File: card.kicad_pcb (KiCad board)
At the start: 2 copper layers, 38.6 x 52.3 mm, 92 parts, among them J1 Conn_01x20_Male, J2 HDMI_A, J3 Conn_01x20_Male, J4 USB_B_Micro, Q1 MMBT3906, Q3 MMBT3906, Q4 MMBT3904, SW1 SW_DPST_x2, U1 SPX3819-1.8, U2 IMP811REUS-T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

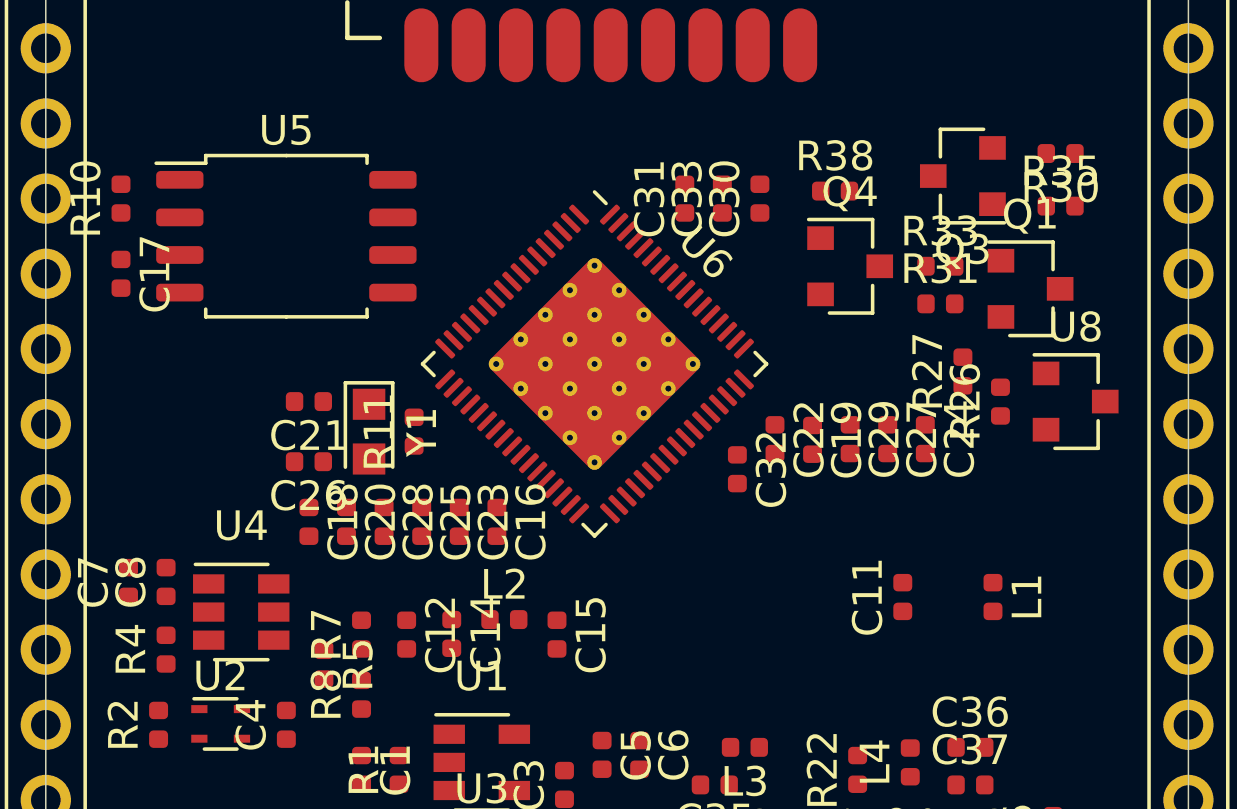
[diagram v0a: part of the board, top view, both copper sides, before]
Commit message: started routing the PCB
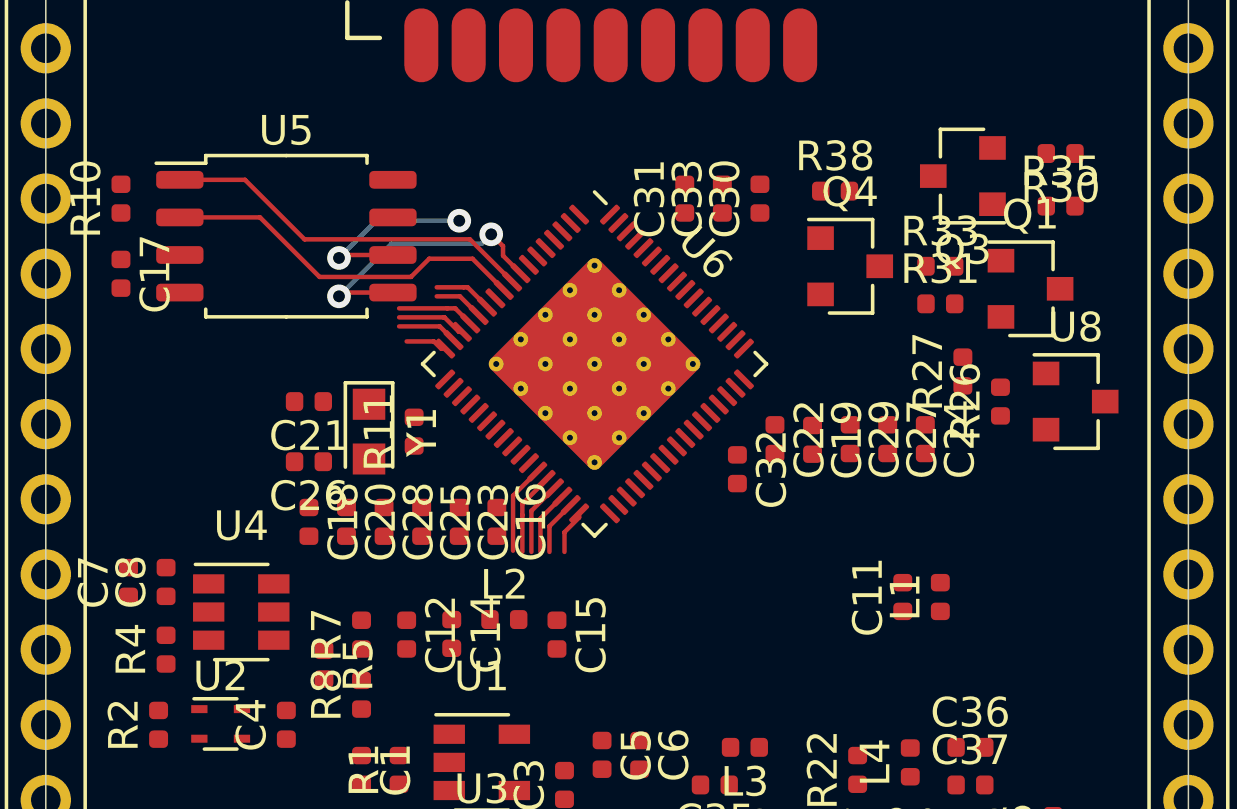
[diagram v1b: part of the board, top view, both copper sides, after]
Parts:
- moved L1 1.78 mm to (264.2, 90.4), turned to 90 degrees
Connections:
- D1 pad 2: Net-(D1-Pad2) -> (no net)
- J2 pad 14: Net-(J2-Pad14) -> (no net)
- J3 pad 8: Net-(J3-Pad8) -> (no net)
- J3 pad 9: Net-(J3-Pad9) -> (no net)
- J4 pad 2: Net-(J4-Pad2) -> (no net)
- J4 pad 3: Net-(J4-Pad3) -> (no net)
- J4 pad 4: Net-(J4-Pad4) -> (no net)
- U6 pad 51: Net-(U6-Pad51) -> (no net)
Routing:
- net /CPU/SPI_CSN: track 0.00 -> 12.7 mm
- net /CPU/SPI_MISO: track 0.00 -> 12.5 mm
- net /CPU/SPI_MOSI: track 0.00 -> 9.61 mm, vias 0 -> 2
- net /CPU/SPI_CLK: track 0.00 -> 6.45 mm, vias 0 -> 2
- net ADCINNQ: track 0.00 -> 3.02 mm
- net ADCINPQ: track 0.00 -> 2.76 mm
- net PORT7: track 0.00 -> 2.62 mm
- net ADCINPI: track 0.00 -> 2.47 mm
- net PORT8: track 0.00 -> 2.32 mm
- net ADCINNI: track 0.00 -> 2.18 mm
- net PORT9: track 0.00 -> 2.03 mm
- net PORT5: track 0.00 -> 1.97 mm
- net HOST0_DP: track 0.00 -> 1.88 mm
- net PORT6: track 0.00 -> 1.68 mm
- net HOST0_DM: track 0.00 -> 1.51 mm
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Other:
- net class Default: clearance 0.2 -> 0.1524; trace_width 0.25 -> 0.1524
- rule trace_clearance: 0.2 -> 0.1524
- rule trace_min: 0.2 -> 0.1524

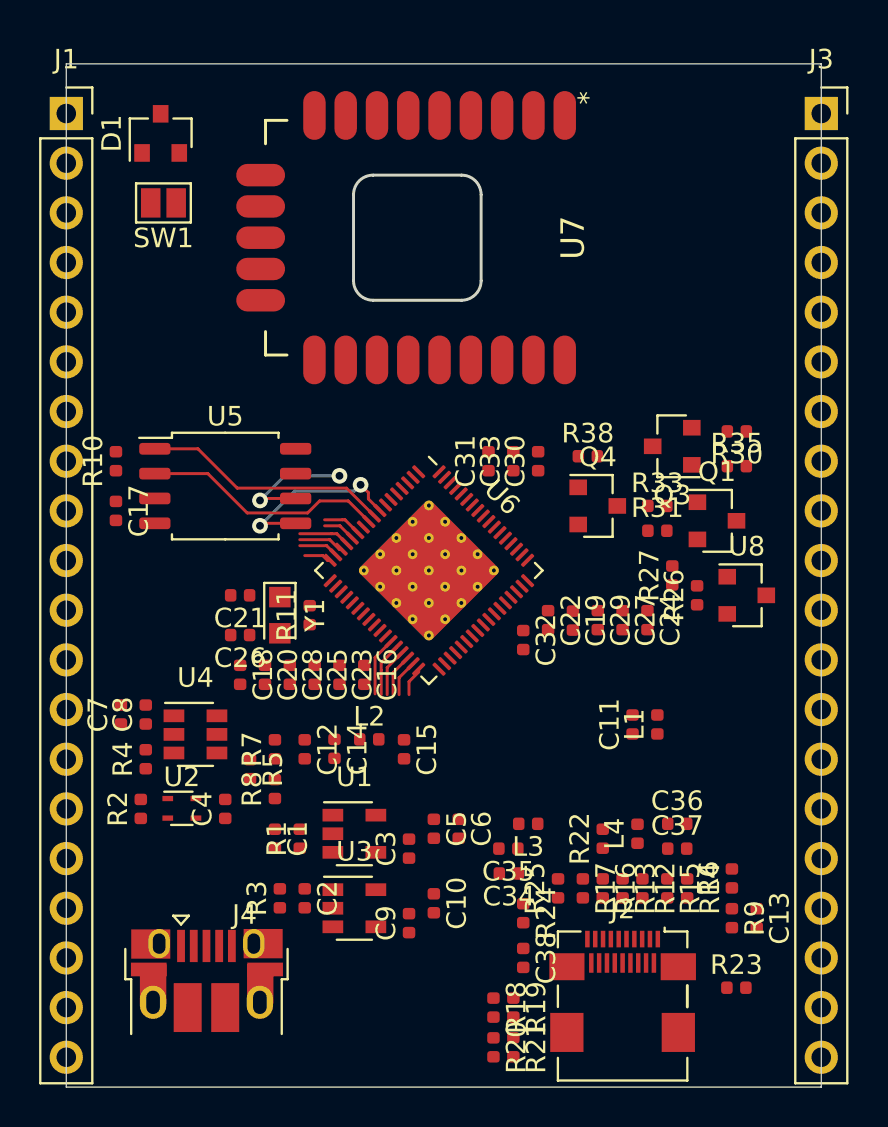
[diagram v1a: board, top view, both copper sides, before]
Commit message: started some routing, removed some useless components
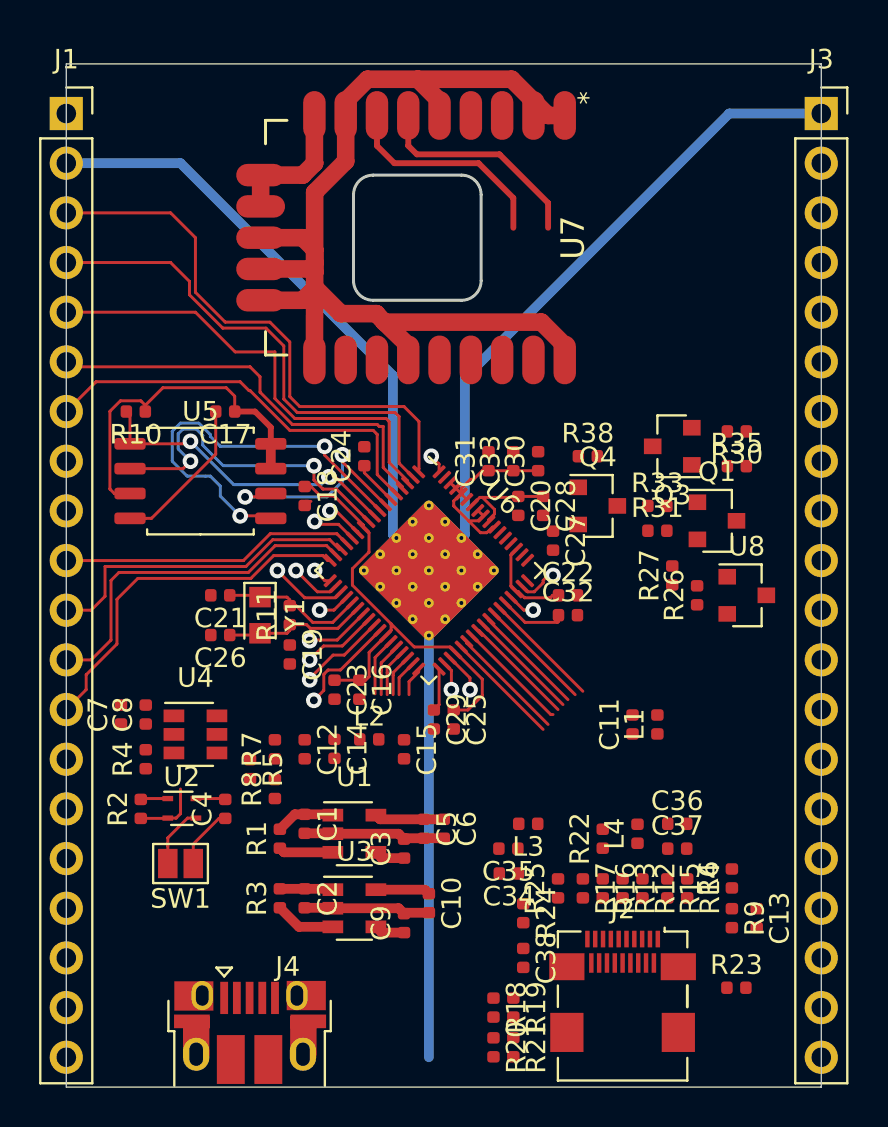
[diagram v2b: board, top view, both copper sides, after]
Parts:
- removed D1: BAT54A, Package_TO_SOT_SMD:SOT-23
- moved SW1 33.8 mm to (239.8, 97.5)
- moved C24 16.7 mm to (249.2, 76.7), turned to 90 degrees
- moved C20 15.6 mm to (257.0, 79.2)
- moved C28 15.6 mm to (258.3, 79.2)
- moved C19 14.6 mm to (245.4, 86.8)
- moved C29 9.80 mm to (252.7, 90.2)
- moved C18 9.72 mm to (246.1, 78.7)
- moved C17 7.55 mm to (242.1, 74.4), turned to 180 degrees
- moved C25 7.47 mm to (253.7, 90.2)
- moved C27 5.40 mm to (258.8, 81.0)
- moved J4 3.45 mm to (243.3, 106.2)
- moved R10 2.74 mm to (237.5, 74.4), turned to 180 degrees
- moved C32 2.62 mm to (259.6, 84.8), turned to 0 degrees
- moved C1 1.70 mm to (246.1, 95.5)
- moved C22 1.63 mm to (259.6, 83.8), turned to 0 degrees
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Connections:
- J3 pad 1: UART1-Rx -> GND
- J3 pad 2: UART1-Tx -> UART1-Rx
- J3 pad 3: GND -> UART1-Tx
- SW1 pad 2: Net-(D1-Pad1) -> MR
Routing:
- net GND: track 0.00 -> 173.0 mm
- net +3V3: track 0.00 -> 33.0 mm, vias 0 -> 1
- net +1V1: track 0.00 -> 29.1 mm
- net PORT0: track 0.00 -> 28.1 mm
- net PORT1: track 0.00 -> 25.4 mm
- net PORT2: track 0.00 -> 23.5 mm
- net PORT3: track 0.00 -> 21.2 mm
- net PORT4: track 0.00 -> 20.7 mm
- net port10: track 1.40 -> 18.3 mm
- net PORT9: track 2.03 -> 17.9 mm
- net PORT8: track 2.32 -> 16.4 mm
- net +1V8: track 0.00 -> 13.9 mm
- net PORT7: track 2.62 -> 14.9 mm
- net /CPU/SPI_MOSI: track 9.61 -> 21.0 mm
- net HOST0_DP: track 1.88 -> 13.1 mm
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
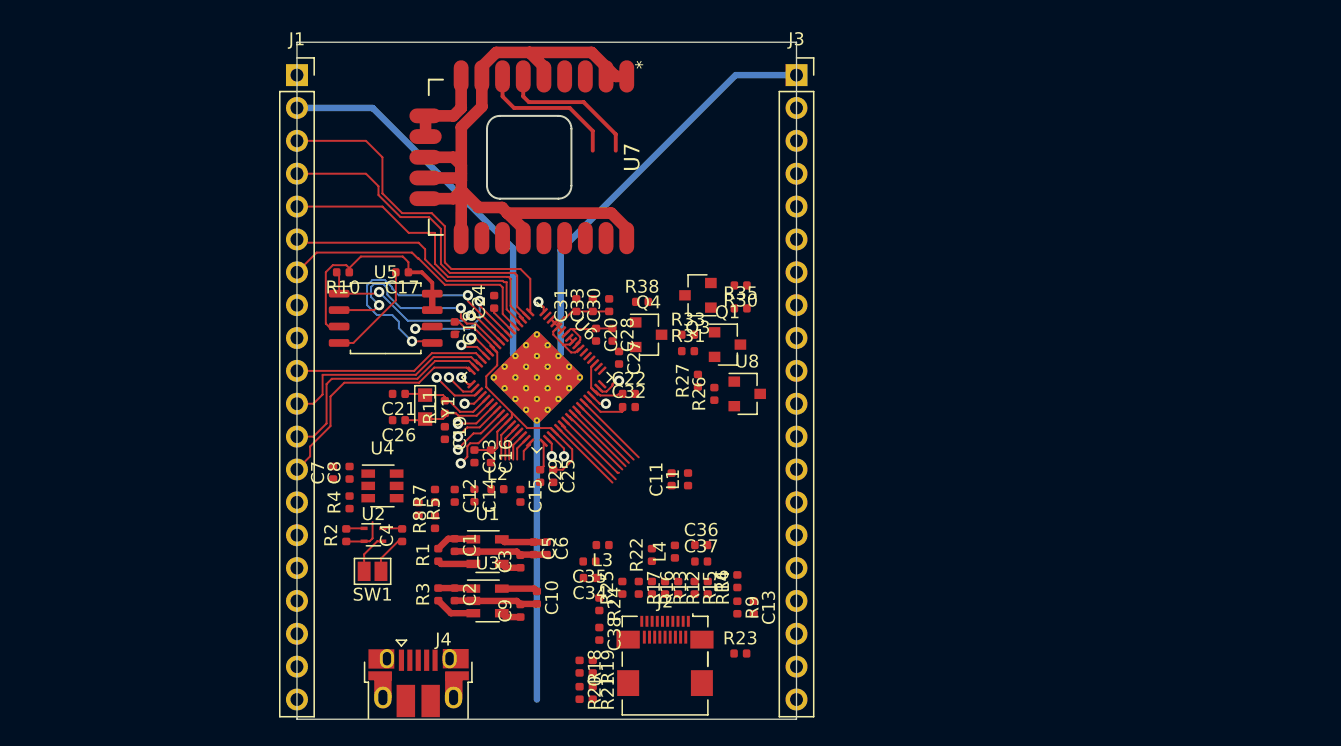
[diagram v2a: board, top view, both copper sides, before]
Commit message: added power allé, and did more routing
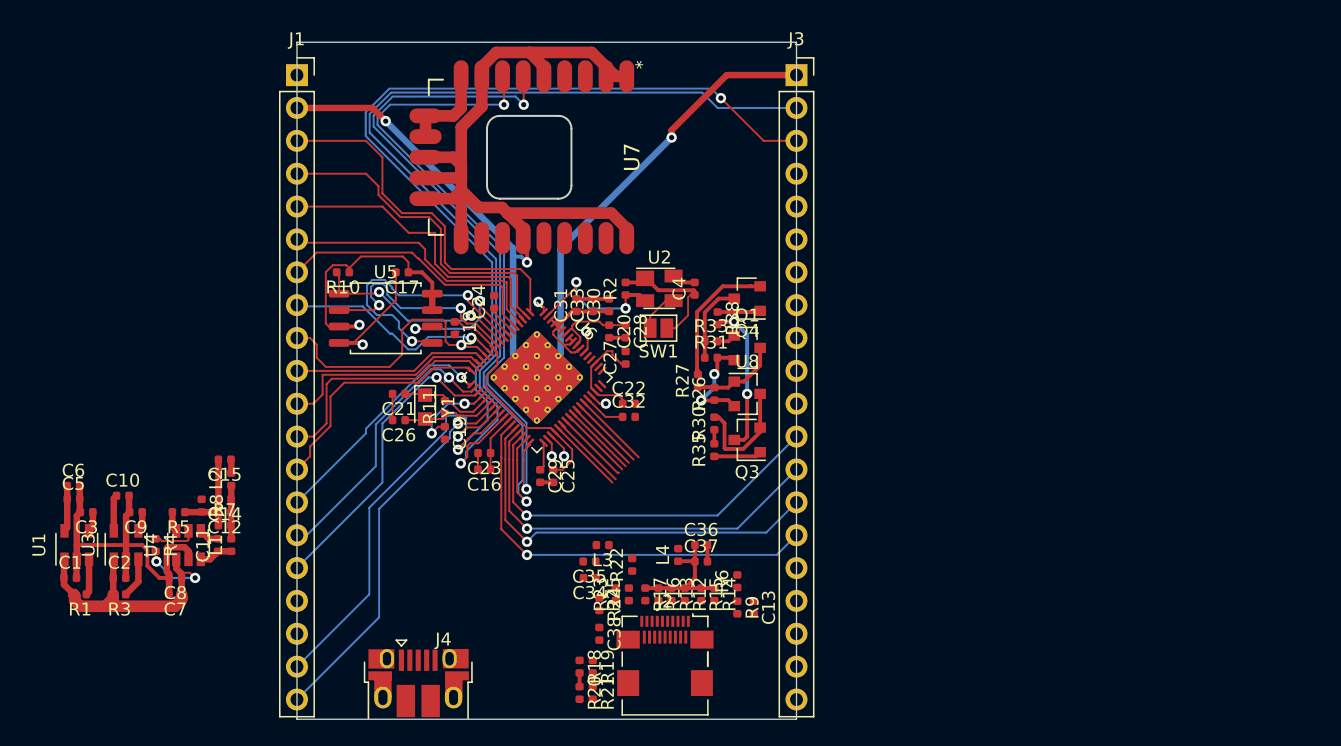
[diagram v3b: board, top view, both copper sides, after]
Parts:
- U2: footprint Package_TO_SOT_SMD:SOT-543 -> Package_TO_SOT_SMD:SOT-143
- moved C6 36.9 mm to (216.7, 90.9), turned to 0 degrees
- moved C5 35.8 mm to (216.7, 91.9), turned to 0 degrees
- moved L1 35.7 mm to (228.9, 95.5)
- moved C11 35.4 mm to (227.8, 95.5)
- moved C3 33.7 mm to (217.7, 93.0), turned to 180 degrees
- moved C10 33.0 mm to (220.5, 91.7), turned to 0 degrees
- moved U1 31.8 mm to (216.9, 95.5), turned to 90 degrees
- moved C9 30.7 mm to (221.5, 93.0), turned to 180 degrees
- moved C1 29.8 mm to (216.4, 98.0), turned to 0 degrees
- moved C4 29.6 mm to (264.7, 75.7)
- moved U2 29.2 mm to (261.9, 75.7)
- moved SW1 29.0 mm to (261.9, 78.7)
- moved R2 28.8 mm to (259.3, 75.7)
- moved U3 28.3 mm to (220.7, 95.5), turned to 90 degrees
- moved R1 27.9 mm to (217.2, 99.3), turned to 180 degrees
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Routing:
- net UART1-Tx: track 4.51 -> 72.0 mm, vias 1 -> 2
- net UART1-Rx: track 5.34 -> 72.6 mm
- net HOST0_DP: track 13.1 -> 56.1 mm, vias 0 -> 2
- net HOST0_DM: track 12.7 -> 51.0 mm, vias 0 -> 2
- net ADCINNQ: track 3.02 -> 32.5 mm, vias 0 -> 1
- net ADCINPQ: track 2.76 -> 31.5 mm, vias 0 -> 1
- net ADCINPI: track 2.47 -> 30.7 mm, vias 0 -> 1
- net ADCINNI: track 2.18 -> 30.0 mm, vias 0 -> 1
- net +5V: track 5.77 -> 33.0 mm, vias 0 -> 4
- net port14-SCL: track 3.89 -> 31.0 mm
- net port15-SDA: track 3.31 -> 29.4 mm
- net GND: track 173.0 -> 194.2 mm, vias 0 -> 4
- net port12: track 2.60 -> 22.2 mm
- net port13: track 3.97 -> 23.2 mm
- net PORT6: track 2.28 -> 20.5 mm
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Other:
- board text added: "Power Allé (AKA ELECTRIC AVINUE)"

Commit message: did more routing
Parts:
- J2: footprint Connector_HDMI:HDMI_Micro-D_Molex_46765-0x01 -> Connector_HDMI:HDMI_A_Contact_Technology_HDMI-19APL2_Horizontal
- J4: footprint Connector_USB:USB_Micro-B_Amphenol_10103594-0001LF_Horizontal -> Connector_USB:USB_Micro-AB_Molex_47590-0001
- moved C13 23.2 mm to (292.1, 96.3)
- moved C34 23.2 mm to (279.4, 94.0)
- moved C36 23.2 mm to (288.0, 91.4)
- moved C37 23.2 mm to (288.0, 92.7)
- moved L3 23.2 mm to (280.4, 91.4)
- moved R12 23.2 mm to (286.8, 95.2)
- moved R13 23.2 mm to (285.8, 95.2)
- moved R14 23.2 mm to (289.1, 95.2)
- moved R15 23.2 mm to (288.0, 95.2)
- moved R17 23.2 mm to (283.7, 95.2)
- moved R22 23.2 mm to (282.7, 93.0)
- moved R23 23.2 mm to (281.4, 95.2)
- moved C35 23.2 mm to (279.4, 92.7)
- moved L4 23.2 mm to (286.3, 92.2)
- moved R6 23.2 mm to (290.8, 94.2)
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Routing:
- net VOUT1: track 0.00 -> 16.5 mm, vias 0 -> 2
- net AOL: track 0.00 -> 4.47 mm, vias 0 -> 1
- net AOR: track 0.00 -> 3.58 mm, vias 0 -> 1
- net (no net): track 0.00 -> 1.74 mm
